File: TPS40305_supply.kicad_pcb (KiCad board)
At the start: 2 copper layers, 31.3 x 48.4 mm, 29 parts, among them J1 Conn_01x01, J2 Conn_01x01, J3 Conn_01x01, J4 Conn_01x01, Q1 CSD16340Q3, Q2 CSD17311Q5, U1 TPS40305

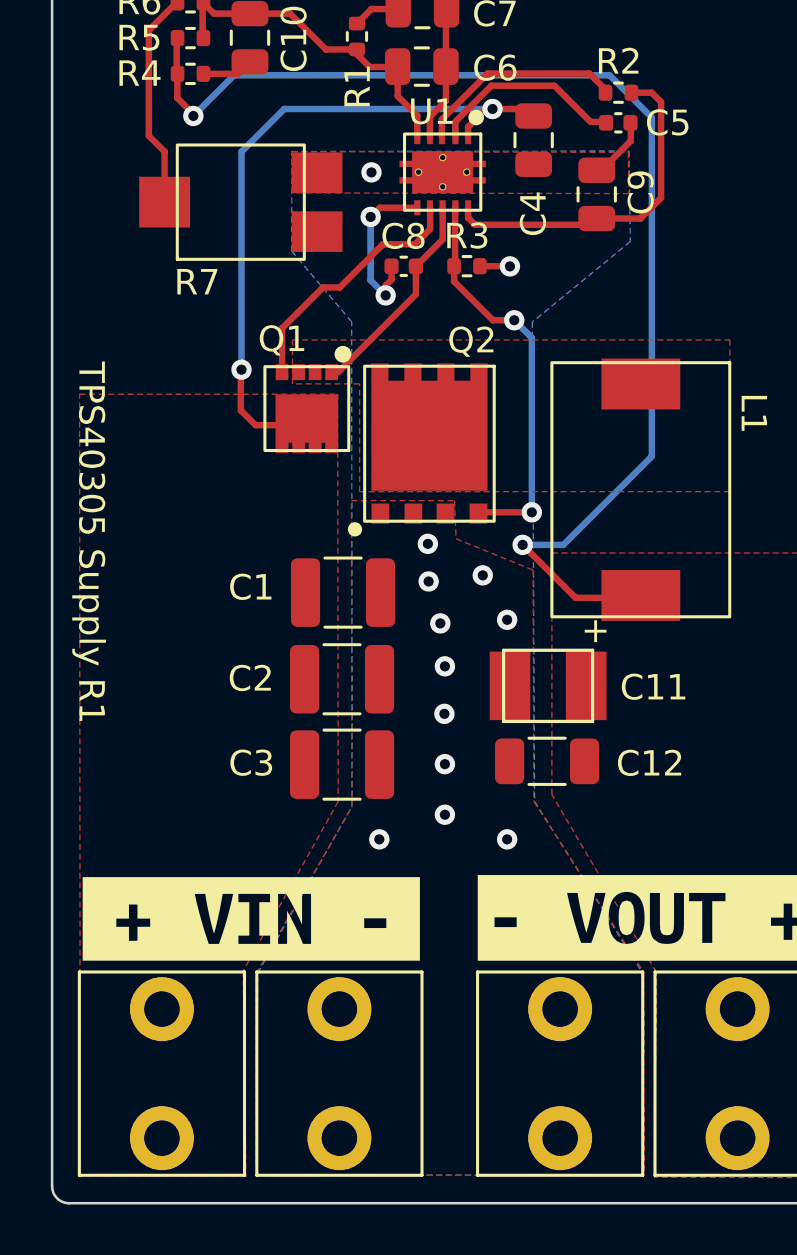
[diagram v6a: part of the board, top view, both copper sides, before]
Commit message: added DK part numbers and generated BOM
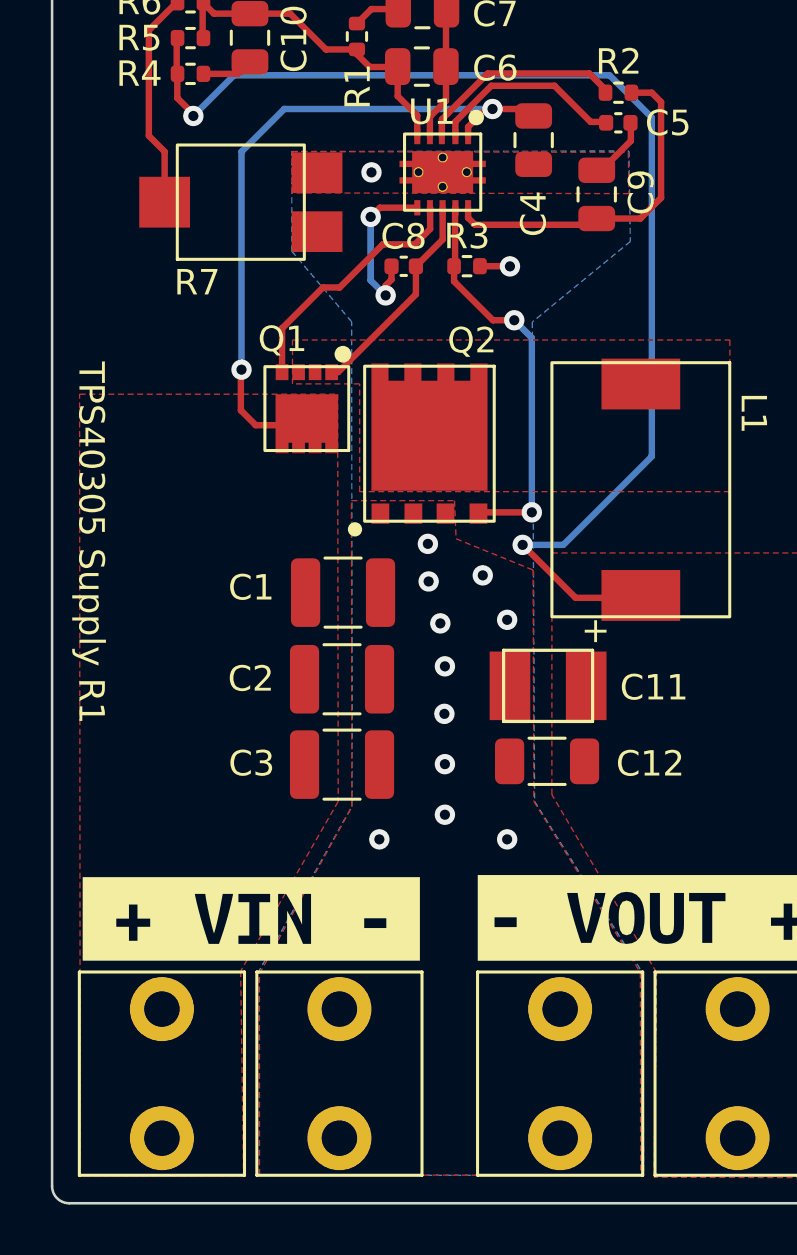
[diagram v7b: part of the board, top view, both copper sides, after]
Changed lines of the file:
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@@
     )
     (fp_poly (pts
-        (xy 0.45 1.7)
-        (xy 0.2 1.7)
-        (xy 0.2 1.33)
-        (xy 0.45 1.33)
+        (xy 0.45 -1.33)
+        (xy 0.2 -1.33)
+        (xy 0.2 -1.7)
+        (xy 0.45 -1.7)
+      ) (layer "F.Paste") (width 0.001) (fill solid))
+    (fp_poly (pts
+        (xy -0.2 -1.33)
+        (xy -0.45 -1.33)
+        (xy -0.45 -1.7)
+        (xy -0.2 -1.7)
+      ) (layer "F.Paste") (width 0.001) (fill solid))
+    (fp_poly (pts
+        (xy -0.2 1.7)
+        (xy -0.45 1.7)
+        (xy -0.45 1.33)
+        (xy -0.2 1.33)
       ) (layer "F.Paste") (width 0.001) (fill solid))
     (fp_poly (pts
@@
       ) (layer "F.Paste") (width 0.001) (fill solid))
     (fp_poly (pts
-        (xy -0.2 1.7)
-        (xy -0.45 1.7)
-        (xy -0.45 1.33)
-        (xy -0.2 1.33)
-      ) (layer "F.Paste") (width 0.001) (fill solid))
-    (fp_poly (pts
-        (xy 0.45 -1.33)
-        (xy 0.2 -1.33)
-        (xy 0.2 -1.7)
-        (xy 0.45 -1.7)
+        (xy 0.45 1.7)
+        (xy 0.2 1.7)
+        (xy 0.2 1.33)
+        (xy 0.45 1.33)
       ) (layer "F.Paste") (width 0.001) (fill solid))
     (fp_poly (pts
@@
         (xy -0.74 0.11)
         (xy 0.71 0.11)
-      ) (layer "F.Paste") (width 0.001) (fill solid))
-    (fp_poly (pts
-        (xy -0.2 -1.33)
-        (xy -0.45 -1.33)
-        (xy -0.45 -1.7)
-        (xy -0.2 -1.7)
       ) (layer "F.Paste") (width 0.001) (fill solid))
     (fp_rect (start -1.5 -1.5) (end 1.5 1.5) (layer "F.SilkS") (width 0.12) (fill none))
@@
     (pad "10" smd roundrect (at 1.4 -1 270) (size 0.6 0.24) (layers "F.Cu" "F.Paste" "F.Mask") (roundrect_rratio 0.03280839895)
       (net 9 "Net-(C9-Pad1)") (pinfunction "BP") (pintype "input"))
-    (pad "11" thru_hole circle (at 0 -0.95 270) (size 0.3 0.3) (drill 0.2) (layers *.Cu *.Mask)
+    (pad "11" thru_hole circle (at 0 0.95 270) (size 0.4 0.4) (drill 0.3) (layers *.Cu *.Mask)
       (net 2 "/GND") (pinfunction "GND") (pintype "input"))
-    (pad "11" thru_hole circle (at 0 0.95 270) (size 0.3 0.3) (drill 0.2) (layers *.Cu *.Mask)
+    (pad "11" thru_hole circle (at 0 -0.95 270) (size 0.4 0.4) (drill 0.3) (layers *.Cu *.Mask)
+      (net 2 "/GND") (pinfunction "GND") (pintype "input"))
+    (pad "11" thru_hole circle (at 0.575 0 270) (size 0.4 0.4) (drill 0.3) (layers *.Cu *.Mask)
       (net 2 "/GND") (pinfunction "GND") (pintype "input"))
     (pad "11" smd custom (at 0 0 270) (size 0.6 0.24) (layers "F.Cu" "F.Mask")
@@
           ) (width 0.001) (fill yes))
       ))
-    (pad "11" thru_hole circle (at -0.575 0 270) (size 0.3 0.3) (drill 0.2) (layers *.Cu *.Mask)
-      (net 2 "/GND") (pinfunction "GND") (pintype "input"))
-    (pad "11" thru_hole circle (at 0.575 0 270) (size 0.3 0.3) (drill 0.2) (layers *.Cu *.Mask)
+    (pad "11" thru_hole circle (at -0.575 0 270) (size 0.4 0.4) (drill 0.3) (layers *.Cu *.Mask)
       (net 2 "/GND") (pinfunction "GND") (pintype "input"))
     (model "${KIPRJMOD}/3D/DRC0010J.stp"
@@
       (pts
         (xy 95.7 73.11)
-        (xy 91.96 79.78)
-        (xy 92.072049 87.86134)
+        (xy 91.862689 79.781349)
+        (xy 91.974738 87.862689)
         (xy 85.547115 87.860614)
         (xy 85.522266 57.079474)
@@
         (xy 103.37 64)
         (xy 103.401 73.1076)
-        (xy 107.73 79.84)
-        (xy 107.741379 87.828105)
-        (xy 92.473923 87.802776)
-        (xy 92.47 79.89)
+        (xy 107.591939 79.840197)
+        (xy 107.603318 87.828302)
+        (xy 92.604213 87.802711)
+        (xy 92.60029 79.889935)
         (xy 96.24 73.32)
         (xy 96.22 61.27)

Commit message: added gerbers
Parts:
- added H1: MountingHole, MountingHole:MountingHole_2.2mm_M2, F.Cu at (113.2, 43.0)
- added H2: MountingHole, MountingHole:MountingHole_2.2mm_M2, F.Cu at (86.9, 73.6)
- added H3: MountingHole, MountingHole:MountingHole_2.2mm_M2, F.Cu at (86.9, 43.0)
- added H4: MountingHole, MountingHole:MountingHole_2.2mm_M2, F.Cu at (113.2, 73.6)
- C8: value 100nF -> 0.1uF
- moved C10 1.71 mm to (93.9, 43.0)
- moved R4 1.71 mm to (91.6, 44.5)
- moved R5 1.71 mm to (91.6, 43.1)
- moved R6 1.71 mm to (91.6, 41.7)
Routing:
- net /VOUT: track 48.2 -> 46.9 mm
- net Net-(C10-Pad2): track 13.2 -> 12.0 mm
- net Net-(R6-Pad2): track 8.58 -> 9.09 mm
